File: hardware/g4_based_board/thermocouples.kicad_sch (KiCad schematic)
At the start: 14 parts, among them U10 MCP3428x-xST, U5 MCP9804_MSOP

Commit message: added more notes on to the sch
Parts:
- C25, C26: footprint Capacitor_SMD:C_0805_2012Metric -> Capacitor_SMD:C_0603_1608Metric_Pad1.08x0.95mm_HandSolder
- R11: footprint Resistor_SMD:R_0805_2012Metric -> Resistor_SMD:R_0603_1608Metric_Pad0.98x0.95mm_HandSolder

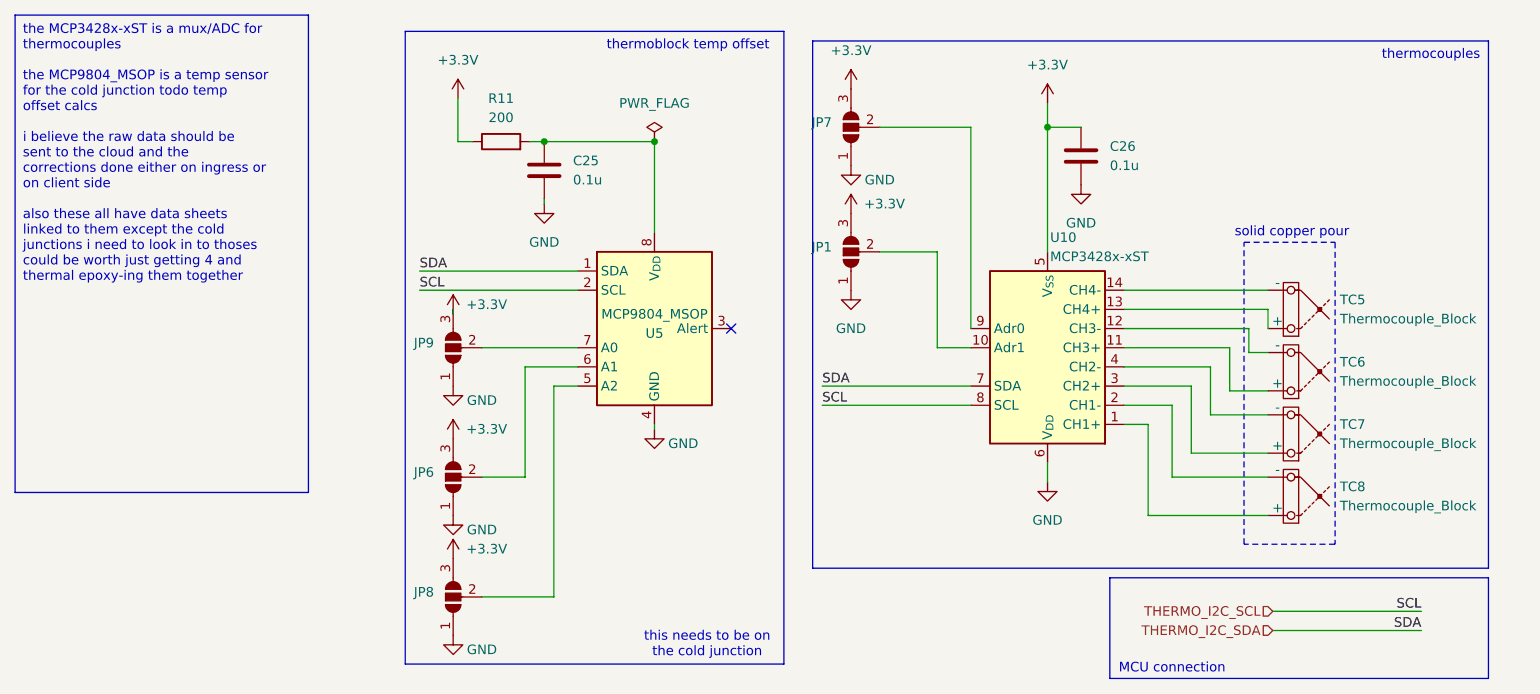
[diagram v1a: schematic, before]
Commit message: swapped around some cold junctions for ease of routing
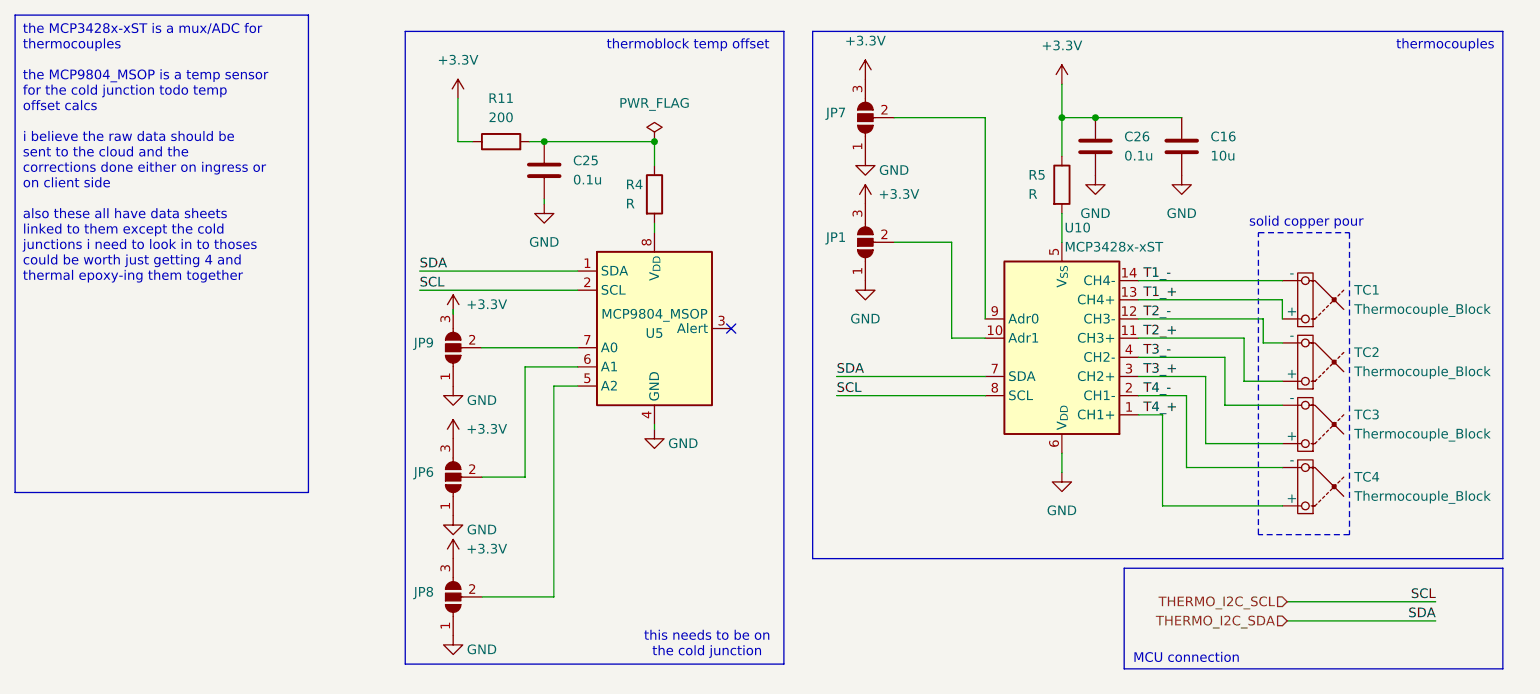
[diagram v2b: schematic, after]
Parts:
- removed TC5, TC6, TC7, TC8: Thermocouple_Block, symbol Device:Thermocouple_Block
- added C16: 10u, Capacitor_SMD:C_0603_1608Metric_Pad1.08x0.95mm_HandSolder, symbol Device:C
- added R4, R5: R, Resistor_SMD:R_0603_1608Metric_Pad0.98x0.95mm_HandSolder, symbol Device:R
- added TC1, TC2, TC3, TC4: Thermocouple_Block, TerminalBlock:TerminalBlock_Altech_AK300-2_P5.00mm, symbol Device:Thermocouple_Block
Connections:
- net +3.3V: now also C16.1, R5.1; no longer U10.5 (V_{SS})
- net GND: now also C16.2
- net T3_+: now reaches U10.3 (CH2+)
- net T3_+: now also TC3.1 (+)
- net T3_-: now reaches U10.4 (CH2-)
- net T3_-: now also TC3.2 (-)
- net at C25.1, R11.2: now also R4.1; no longer U5.8 (V_{DD})
- net T2_+: now reaches U10.11 (CH3+)
- net T2_+: now also TC2.1 (+)
- net T2_-: now reaches U10.12 (CH3-)
- net T2_-: now also TC2.2 (-)
- net T4_+: now reaches U10.1 (CH1+)
- net T4_+: now also TC4.1 (+)
- net T1_+: now reaches U10.13 (CH4+)
- net T1_+: now also TC1.1 (+)
- net T1_-: now reaches U10.14 (CH4-)
- net T1_-: now also TC1.2 (-)
- net T4_-: now reaches U10.2 (CH1-)
- net T4_-: now also TC4.2 (-)
- new net: R5.2, U10.5 (V_{SS})
- new net: R4.2, U5.8 (V_{DD})
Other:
- moved on the sheet: C26, JP1, JP7, U10

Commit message: swapped thermocouple layout yet again
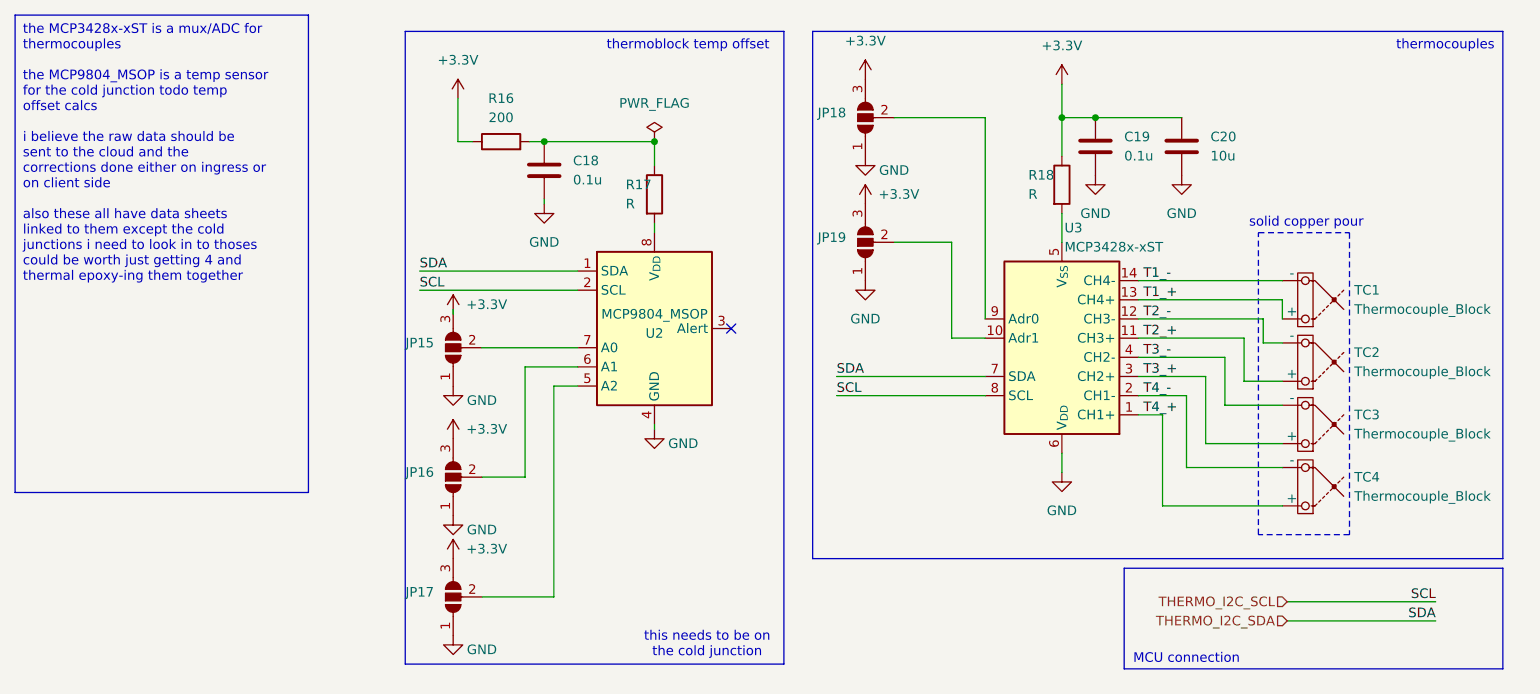
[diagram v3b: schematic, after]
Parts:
- renumbered C25 to C18, C26 to C19, C16 to C20, JP9 to JP15, JP6 to JP16, JP8 to JP17, JP7 to JP18, JP1 to JP19, R11 to R16, R4 to R17, R5 to R18, U5 to U2, U10 to U3

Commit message: rev-1
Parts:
- R17, R18: value R -> 0
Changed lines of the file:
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@@
 		(dnp no)
 		(property "Reference" "R17"
-			(at 104.775 85.725 0)
+			(at 111.125 86.36 0)
 			(effects
 				(font
@@
 			)
 		)
-		(property "Value" "R"
-			(at 104.775 88.265 0)
+		(property "Value" "0"
+			(at 111.125 88.9 0)
 			(effects
 				(font
@@
 		(dnp no)
 		(property "Reference" "R18"
-			(at 158.115 84.455 0)
+			(at 156.845 84.455 0)
 			(effects
 				(font
@@
 			)
 		)
-		(property "Value" "R"
+		(property "Value" "0"
 			(at 158.115 86.995 0)
 			(effects
